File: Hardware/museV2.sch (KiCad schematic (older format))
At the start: 88 parts

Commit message: Added Lighting Connectors
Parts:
- removed P? (x16): CONN_01X03, symbol CONN_01X03
- added P? (x4): CONN_01X04, symbol CONN_01X04
- added P? (x16): AI_RGB, symbol CONN_01X03
- added Q? (x12): MOSFET_N, symbol MOSFET_N
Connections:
- wire segments 365 -> 584
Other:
- note added: "Individually \nAddressable\nRGB LED Strips"
- note added: "Single RGB LED Strips"
- moved on the sheet: C?, R?, U?, X?

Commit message: Added missing i2s pins to Edison
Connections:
- net Audio_Filter/ANALOG_OUT+ is gone; now on net Audio_Filter/ANALOG_OUT+: U?.25 (IOUT_L+)
- net Audio_Filter/ANALOG_OUT- is gone; now on net Audio_Filter/ANALOG_OUT-: U?.26 (IOUT_L-)
- net I2C_SCK is gone; now on net I2C_SCL: U?.12 (MC)
- net Audio_Filter/ANALOG_OUT+: no longer U?.17 (IOUT_R+)
- net Audio_Filter/ANALOG_OUT-: no longer U?.18 (IOUT_R-)
- net I2C_SCL: now also U?.41 (GP19_I2C_1_SCL)
- net I2C_SCA: now reaches U?.43 (GP20_I2C_1_SDA)
- new net Audio_Filter/ANALOG_OUT+: U?.17 (IOUT_R+)
- new net Audio_Filter/ANALOG_OUT-: U?.18 (IOUT_R-)
- no-connect marks 42 -> 40
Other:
- note added: "To DFE/\n ADC/\n DAC"

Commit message: Added Microphones and Mic Bias
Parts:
- added C? (x4): 10uF, symbol C
- added C?: 0.1uF, symbol C
- added R? (x4): 100K, symbol R
- added R? (x4): 2.2K, symbol R
- added U? (x4): POM-3535L-3-R, symbol POM-3535L-3-R
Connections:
- net Audio_Filter/ANALOG_OUT+ is gone; now on net Audio_Filter/ANALOG_OUT+: U?.25 (IOUT_L+)
- net Audio_Filter/ANALOG_OUT- is gone; now on net Audio_Filter/ANALOG_OUT-: U?.26 (IOUT_L-)
- net 3.5_IN_L: now also R?.1
- net 3.5_IN_R: now also R?.1
- net Audio_Filter/ANALOG_OUT+: no longer U?.17 (IOUT_R+)
- net Audio_Filter/ANALOG_OUT-: no longer U?.18 (IOUT_R-)
- net GND: now also C?.2, R?.2, R?.2, R?.2, R?.2, U?.~ (PWR), U?.~ (PWR), U?.~ (PWR), U?.~ (PWR)
- net RCA_IN_L: now also R?.1
- net RCA_IN_R: now also R?.1
- net ADC_ESEN_INT: now reaches U?.47 (GP28_I2C_6_SDA)
- net ADC_ESEN_INT: now also U?.21 (GPIO_1/Int_A/DMIN)
- net at C?.1, U?.1 (VINL2/VIN1M): no longer R?.1
- net at C?.1, U?.2 (VINR2/VIN2M): no longer R?.1
- net at U?.27 (VINL4/VIN4M): now also C?.1
- net at U?.28 (VINR4/VIN3M): now also C?.1
- net at U?.29 (VINL3/VIN4P): now also C?.1
- net at C?.1, U?.3 (VINL1/VIN1P): no longer R?.1
- net at U?.30 (VINR3/VIN3P): now also C?.1
- net at C?.1, U?.4 (VINR1/VIN2P): no longer R?.1
- net at U?.5 (Mic_Bias): now also C?.1, R?.2, R?.2, R?.2, R?.2
- new net Audio_Filter/ANALOG_OUT+: U?.17 (IOUT_R+)
- new net Audio_Filter/ANALOG_OUT-: U?.18 (IOUT_R-)
- new net MIC_1: C?.2, R?.1, R?.1, U?.~ (PWR)
- new net MIC_2: C?.2, R?.1, R?.1, U?.~ (PWR)
- new net MIC_3: C?.2, R?.1, R?.1, U?.~ (PWR)
- new net MIC_4: C?.2, R?.1, R?.1, U?.~ (PWR)
- no-connect marks 40 -> 33
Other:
- note added: "Microphones"
- moved on the sheet: C?, P?, Q?, R?, U?

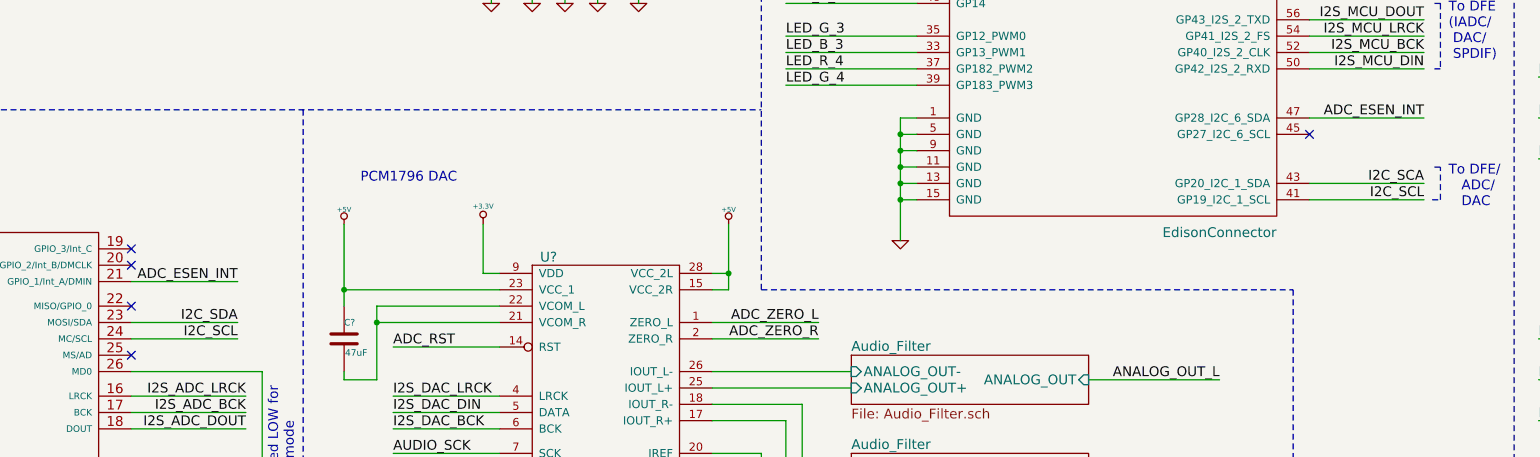
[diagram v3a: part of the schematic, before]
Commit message: Added ADC interrupt output pins to Edison
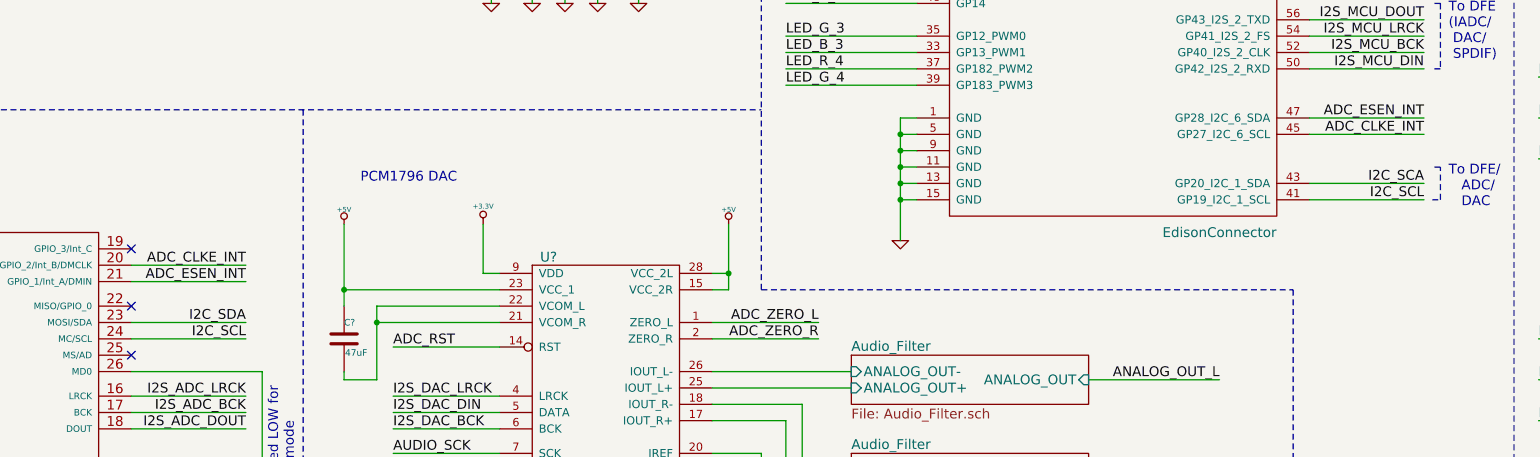
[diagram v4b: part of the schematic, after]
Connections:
- net Audio_Filter/ANALOG_OUT+ is gone; now on net Audio_Filter/ANALOG_OUT+: U?.25 (IOUT_L+)
- net Audio_Filter/ANALOG_OUT- is gone; now on net Audio_Filter/ANALOG_OUT-: U?.26 (IOUT_L-)
- net Audio_Filter/ANALOG_OUT+: no longer U?.17 (IOUT_R+)
- net Audio_Filter/ANALOG_OUT-: no longer U?.18 (IOUT_R-)
- net ADC_CLKE_INT: now reaches U?.45 (GP27_I2C_6_SCL)
- net ADC_CLKE_INT: now also U?.20 (GPIO_2/Int_B/DMCLK)
- new net Audio_Filter/ANALOG_OUT+: U?.17 (IOUT_R+)
- new net Audio_Filter/ANALOG_OUT-: U?.18 (IOUT_R-)
- no-connect marks 33 -> 31
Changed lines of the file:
@@
 Text Label 8700 6150 0    60   ~ 0
 LED_R_1
-NoConn ~ 11900 7550
 Text Notes 6950 1900 0    60   ~ 0
 Optical Output
@@
 NoConn ~ 6950 9950
 NoConn ~ 4700 8600
-Text Label 5350 8700 2    60   ~ 0
+Text Label 5400 8700 2    60   ~ 0
 I2C_SDA
-Text Label 5350 8800 2    60   ~ 0
+Text Label 5400 8800 2    60   ~ 0
 I2C_SCL
 Text Notes 5700 9700 1    60   ~ 0
@@
 NoConn ~ 9500 4050
 NoConn ~ 4700 8250
-NoConn ~ 4700 8350
 Text Label 12600 7150 2    60   ~ 0
 I2S_MCU_DIN
@@
 Text Notes 12750 8000 0    60   ~ 0
 To DFE/\n   ADC/\n   DAC
-Text Label 5350 8450 2    60   ~ 0
+Text Label 5400 8450 2    60   ~ 0
 ADC_ESEN_INT
 Text Label 12600 7450 2    60   ~ 0
@@
 	6000 10000 6000 10100
 Wire Wire Line
-	4700 8700 5350 8700
+	4700 8700 5400 8700
 Wire Wire Line
 	5500 9000 5500 10950
@@
 	4700 9000 5500 9000
 Wire Wire Line
-	4700 8800 5350 8800
+	4700 8800 5400 8800
 Wire Wire Line
 	950  6050 1850 6050
@@
 	12700 7750 12650 7750
 Wire Wire Line
-	4700 8450 5350 8450
+	4700 8450 5400 8450
 Wire Wire Line
 	11900 7450 12600 7450
@@
 Wire Wire Line
 	1400 10400 1400 9500
+Wire Wire Line
+	4700 8350 5400 8350
+Text Label 5400 8350 2    60   ~ 0
+ADC_CLKE_INT
+Wire Wire Line
+	11900 7550 12600 7550
+Text Label 12600 7550 2    60   ~ 0
+ADC_CLKE_INT
 $EndSCHEMATC

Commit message: Corrected DFE GPIO Data Port Connections
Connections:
- net Audio_Filter/ANALOG_OUT+ is gone; now on net Audio_Filter/ANALOG_OUT+: U?.25 (IOUT_L+)
- net Audio_Filter/ANALOG_OUT- is gone; now on net Audio_Filter/ANALOG_OUT-: U?.26 (IOUT_L-)
- net Audio_Filter/ANALOG_OUT+: no longer U?.17 (IOUT_R+)
- net Audio_Filter/ANALOG_OUT-: no longer U?.18 (IOUT_R-)
- net I2S_MCU_BCK: now also U?.9 (GPIO_C2); no longer U?.5 (GPIO_A2)
- net I2S_MCU_DOUT: now also U?.7 (GPIO_C0); no longer U?.3 (GPIO_A0)
- net I2S_MCU_LRCK: now also U?.8 (GPIO_C1); no longer U?.4 (GPIO_A1)
- net I2S_SCK: now also U?.10 (GPIO_C3); no longer U?.6 (GPIO_A3)
- new net Audio_Filter/ANALOG_OUT+: U?.17 (IOUT_R+)
- new net Audio_Filter/ANALOG_OUT-: U?.18 (IOUT_R-)
- no-connect marks 31 -> 36

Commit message: Added LED Strip Current Limiting Resistor
Added PSU surge protection caps
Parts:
- added C? (x4): 1000uF, symbol C
- added R? (x6): 470, symbol R
- gave numbers to parts that had none: 121
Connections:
- net Audio_Filter/ANALOG_OUT+ is gone; now on net Audio_Filter/ANALOG_OUT+: U11.25 (IOUT_L+)
- net Audio_Filter/ANALOG_OUT- is gone; now on net Audio_Filter/ANALOG_OUT-: U11.26 (IOUT_L-)
- net +12V: now also C?.1, C?.1
- net +5V: now also C?.1, C?.1
- net Audio_Filter/ANALOG_OUT+: no longer U11.17 (IOUT_R+)
- net Audio_Filter/ANALOG_OUT-: no longer U11.18 (IOUT_R-)
- net GND: now also C?.2, C?.2, C?.2, C?.2
- net LED_IA_1: now also R?.2; no longer P6.2 (P2)
- net LED_IA_2: now also R?.2; no longer P8.2 (P2)
- net LED_IA_3: now also R?.2; no longer P9.2 (P2)
- net LED_IA_4: now also R?.2; no longer P10.2 (P2)
- net LED_IA_5: now also R?.2; no longer P11.2 (P2)
- net LED_IA_6: now also R?.2; no longer P13.2 (P2)
- new net: P6.2 (P2), R?.1
- new net: P8.2 (P2), R?.1
- new net: P9.2 (P2), R?.1
- new net: P10.2 (P2), R?.1
- new net: P11.2 (P2), R?.1
- new net: P13.2 (P2), R?.1
- new net Audio_Filter/ANALOG_OUT+: U11.17 (IOUT_R+)
- new net Audio_Filter/ANALOG_OUT-: U11.18 (IOUT_R-)
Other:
- note added: "PSU Surge Supress"
- moved on the sheet: C1, C10, C11, C12, C13, C14, C15, C16, C17, C18, C19, C2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

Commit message: Added Aux ATX Power connector, reorganized layout
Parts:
- removed C? (x2): 1000uF, symbol C
- added J?: ATX24, symbol ATX24
- added R? (x10): 470, symbol R
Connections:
- net Audio_Filter/ANALOG_OUT+ is gone; now on net Audio_Filter/ANALOG_OUT+: U11.25 (IOUT_L+)
- net Audio_Filter/ANALOG_OUT- is gone; now on net Audio_Filter/ANALOG_OUT-: U11.26 (IOUT_L-)
- net +12V: now also J?.10 (12V), J?.11 (12V)
- net +5V: now also J?.21 (5V), J?.22 (5V), J?.23 (5V), J?.4 (5V), J?.6 (5V)
- net ATX_PS_ON: now also J?.16 (PS_ON)
- net Audio_Filter/ANALOG_OUT+: no longer U11.17 (IOUT_R+)
- net Audio_Filter/ANALOG_OUT-: no longer U11.18 (IOUT_R-)
- net GND: now also J?.15 (GND), J?.17 (GND), J?.18 (GND), J?.19 (GND), J?.24 (GND), J?.3 (GND), J?.5 (GND), J?.7 (GND)
- net LED_IA_10: now also R?.2; no longer P18.2 (P2)
- net LED_IA_11: now also R?.2; no longer P19.2 (P2)
- net LED_IA_12: now also R?.2; no longer P20.2 (P2)
- net LED_IA_13: now also R?.2; no longer P21.2 (P2)
- net LED_IA_14: now also R?.2; no longer P23.2 (P2)
- net LED_IA_15: now also R?.2; no longer P24.2 (P2)
- net LED_IA_16: now also R?.2; no longer P25.2 (P2)
- net LED_IA_7: now also R?.2; no longer P14.2 (P2)
- net LED_IA_8: now also R?.2; no longer P15.2 (P2)
- net LED_IA_9: now also R?.2; no longer P16.2 (P2)
- new net: P14.2 (P2), R?.1
- new net: P15.2 (P2), R?.1
- new net: P16.2 (P2), R?.1
- new net: P18.2 (P2), R?.1
- new net: P19.2 (P2), R?.1
- new net: P20.2 (P2), R?.1
- new net: P21.2 (P2), R?.1
- new net: P23.2 (P2), R?.1
- new net: P24.2 (P2), R?.1
- new net: P25.2 (P2), R?.1
- new net AUX_PS_OK: J?.8 (POK)
- new net Audio_Filter/ANALOG_OUT+: U11.17 (IOUT_R+)
- new net Audio_Filter/ANALOG_OUT-: U11.18 (IOUT_R-)
- no-connect marks 36 -> 43
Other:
- note added: "ATX Power Connectors"
- note added: "Edison UART \nInterface"
- note removed: "ATX Power Connector"
- note removed: "Edison UART Interface"
- moved on the sheet: C1, C10, C11, C12, C13, C14, C15, C16, C17, C18, C19, C2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

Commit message: Annotated
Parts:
- gave numbers to parts that had none: 19
- renumbered C33 to C35, C34 to C36, C35 to C37, C36 to C38, C37 to C39, C38 to C40, C39 to C41, C40 to C42, C41 to C43, C42 to C44, C43 to C45, C44 to C46, C45 to C47, C46 to C48, C47 to C49, C48 to C50, C49 to C51, C50 to C52, C51 to C53, P3 to P2, P4 to P3, P2 to P4, R4 to R11, R5 to R18, R6 to R19, R7 to R20, R8 to R21, R9 to R25, R10 to R26, R11 to R27, R12 to R28, R13 to R29, R14 to R30, R15 to R31, R16 to R32, R17 to R33, R1 to R6, R2 to R8, R3 to R9
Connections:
- net Audio_Filter/ANALOG_OUT+ is gone; now on net Audio_Filter/ANALOG_OUT+: U11.25 (IOUT_L+)
- net Audio_Filter/ANALOG_OUT- is gone; now on net Audio_Filter/ANALOG_OUT-: U11.26 (IOUT_L-)
- net Audio_Filter/ANALOG_OUT+: no longer U11.17 (IOUT_R+)
- net Audio_Filter/ANALOG_OUT-: no longer U11.18 (IOUT_R-)
- new net Audio_Filter/ANALOG_OUT+: U11.17 (IOUT_R+)
- new net Audio_Filter/ANALOG_OUT-: U11.18 (IOUT_R-)
